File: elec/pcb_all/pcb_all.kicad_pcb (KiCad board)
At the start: 2 copper layers, 1 part, among them U1 Xiao_ESP32-C3

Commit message: did most pf power schematics
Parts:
- added IC1: BQ25176MDSGR, footprints:SON50P200X200X80-9N, F.Cu at (99.2, 59.5)
- added U2: BQ29700DSER, footprints:SON50P150X150X80-6N, F.Cu at (96.6, 71.2)

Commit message: did pcb layout for bucks, boost, imu, barometer, vibration module, need to continue batt protection
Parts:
- added B1: HD-EMC1003-3-LW27, footprints:PUI_HD-EMC1003-3-LW27, F.Cu at (89.1, 167.3)
- added BT1: Battery_Cell, Connector_JST:JST_XH_B2B-XH-A_1x02_P2.50mm_Vertical, F.Cu at (107.5, 103.0)
- added C1: 4.7uF, Capacitor_SMD:C_1206_3216Metric, F.Cu at (91.2, 127.5)
- added C10: 22uF, Capacitor_SMD:C_1206_3216Metric, F.Cu at (111.4, 124.8)
- added C11: 10uF, Capacitor_SMD:C_1206_3216Metric, F.Cu at (88.0, 106.8)
- added C12: 1uF, Capacitor_SMD:C_0603_1608Metric, F.Cu at (83.0, 40.0)
- added C13: 22uF, Capacitor_SMD:C_1206_3216Metric, F.Cu at (93.0, 100.5)
- added C14: 100nF, Capacitor_SMD:C_0603_1608Metric, F.Cu at (83.0, 42.6)
- added C15: 22uF, Capacitor_SMD:C_1206_3216Metric, F.Cu at (90.2, 100.5)
- added C16: 10uF, Capacitor_SMD:C_1206_3216Metric, F.Cu at (105.5, 43.0)
- added C17: 0.1uF, Capacitor_SMD:C_0603_1608Metric, F.Cu at (107.5, 165.5)
- added C18: 100nF, Capacitor_SMD:C_0603_1608Metric, F.Cu at (88.2, 145.8)
- added C19: 100nF, Capacitor_SMD:C_0603_1608Metric, F.Cu at (106.4, 151.6)
- added C2: 0.1uF, Capacitor_SMD:C_0603_1608Metric, F.Cu at (124.0, 101.0)
- added C20: 22uF, Capacitor_SMD:C_1206_3216Metric, F.Cu at (108.2, 162.2)
- added C21: 100nF, Capacitor_SMD:C_0603_1608Metric, F.Cu at (91.5, 148.8)
- added C22: 100nF, Capacitor_SMD:C_0603_1608Metric, F.Cu at (109.7, 148.3)
- added C3: 22uF, Capacitor_SMD:C_1206_3216Metric, F.Cu at (87.7, 130.8)
- added C4: 10uF, Capacitor_SMD:C_1206_3216Metric, F.Cu at (101.4, 125.1)
- added C5: 1uF, Capacitor_SMD:C_0603_1608Metric, F.Cu at (83.0, 35.0)
- added C6: 100nF, Capacitor_SMD:C_0201_0603Metric, F.Cu at (105.7, 127.8)
- added C7: 100nF, Capacitor_SMD:C_0603_1608Metric, F.Cu at (83.0, 37.5)
- added C8: 22uF, Capacitor_SMD:C_1206_3216Metric, F.Cu at (108.9, 124.8)
- added C9: 10uF, Capacitor_SMD:C_1206_3216Metric, F.Cu at (99.9, 46.3)
- added D1: ESD7351XV2T1G, footprints:SODFL1608X70N, F.Cu at (77.0, 53.8)
- added D2: LED, Capacitor_SMD:C_0603_1608Metric, F.Cu at (87.0, 35.0)
- added D3: LED, Capacitor_SMD:C_0603_1608Metric, F.Cu at (87.0, 37.5)
- added D4: LED, Capacitor_SMD:C_0603_1608Metric, F.Cu at (87.0, 40.0)
- added D5: ESD7351XV2T1G, footprints:SODFL1608X70N, F.Cu at (77.0, 56.1)
- added D6: LED, Capacitor_SMD:C_0603_1608Metric, F.Cu at (87.0, 42.6)
- added D7: SS14-M3_5AT, footprints:DIOM5127X229N, F.Cu at (104.3, 167.2)
- added IC2: AP63203WU-7, footprints:AP63203WU7, F.Cu at (105.2, 124.8)
- added IC3: BQ25176MDSGR, footprints:SON50P200X200X80-9N, F.Cu at (67.9, 67.1)
- added IC4: TPS61023DRLR, footprints:SOTFL50P160X60-6N, F.Cu at (87.8, 101.8)
- added IC5: BMP390, footprints:BMP390, F.Cu at (88.0, 149.2)
- added IC6: LSM6DSLTR, footprints:LSM6DSLTR, F.Cu at (106.2, 148.6)
- added J1: Conn_01x02, Connector_JST:JST_XH_B2B-XH-A_1x02_P2.50mm_Vertical, F.Cu at (104.3, 65.0)
- added J2: Conn_01x07, Connector_PinHeader_2.54mm:PinHeader_1x07_P2.54mm_Vertical, F.Cu at (63.4, 50.4)
- added L1: 2.2uH, Inductor_SMD:L_1008_2520Metric, F.Cu at (85.7, 126.8)
- added L2: 4.7uH, Inductor_SMD:L_1008_2520Metric, F.Cu at (106.4, 129.6)
- added L3: 1uH, Inductor_SMD:L_1008_2520Metric, F.Cu at (88.5, 104.3)
- added Q1: CSD16301Q2, footprints:CSD16301Q2, F.Cu at (126.5, 105.2)
- added Q2: CSD16301Q2, footprints:CSD16301Q2, F.Cu at (119.8, 105.2)
- added Q3: IRLML6344TRPBF, footprints:SOT95P237X112-3N, F.Cu at (108.0, 168.2)
- added R1: 34k, Resistor_SMD:R_0603_1608Metric, F.Cu at (89.4, 123.7)
- added R10: 10k, Resistor_SMD:R_0603_1608Metric, F.Cu at (91.0, 45.1)
- added R11: 680R, Resistor_SMD:R_0603_1608Metric, F.Cu at (91.0, 47.6)
- added R12: 10k, Resistor_SMD:R_0603_1608Metric, F.Cu at (91.0, 50.1)
- added R13: 604, Resistor_SMD:R_0603_1608Metric, F.Cu at (91.0, 52.6)
- added R14: 24.3k, Resistor_SMD:R_0603_1608Metric, F.Cu at (95.0, 32.5)
- added R15: 732k, Resistor_SMD:R_0603_1608Metric, F.Cu at (86.0, 100.0)
- added R16: 100k, Resistor_SMD:R_0603_1608Metric, F.Cu at (85.8, 102.3)
- added R17: 680R, Resistor_SMD:R_0603_1608Metric, F.Cu at (95.0, 40.0)
- added R18: 10k, Resistor_SMD:R_0603_1608Metric, F.Cu at (95.0, 42.6)
- added R19: 1k, Resistor_SMD:R_0603_1608Metric, F.Cu at (95.0, 45.1)
- added R2: 4.7k, Resistor_SMD:R_0603_1608Metric, F.Cu at (87.0, 47.6)
- added R20: 10k, Resistor_SMD:R_0603_1608Metric, F.Cu at (110.8, 165.5)
- added R21: 100R, Resistor_SMD:R_0603_1608Metric, F.Cu at (111.8, 168.2)
- added R22: 4.7k, Resistor_SMD:R_0603_1608Metric, F.Cu at (106.7, 144.6)
- added R3: R330, Resistor_SMD:R_0603_1608Metric, F.Cu at (126.0, 101.0)
- added R4: 4.7k, Resistor_SMD:R_0603_1608Metric, F.Cu at (87.0, 52.6)
- added R5: 64.9k, Resistor_SMD:R_0603_1608Metric, F.Cu at (87.9, 123.7)
- added R6: 5.1M, Resistor_SMD:R_0603_1608Metric, F.Cu at (121.8, 101.8)
- added R7: 5.1M, Resistor_SMD:R_0603_1608Metric, F.Cu at (118.8, 101.0)
- added R8: 2.2K, Resistor_SMD:R_0603_1608Metric, F.Cu at (128.0, 101.0)
- added R9: 10k, Resistor_SMD:R_0603_1608Metric, F.Cu at (91.0, 42.6)
- added TP1: TestPoint_2Pole, Connector_PinHeader_2.54mm:PinHeader_1x02_P2.54mm_Vertical, F.Cu at (105.0, 94.2)
- added TP2: TestPoint, Connector_PinHeader_2.54mm:PinHeader_1x01_P2.54mm_Vertical, F.Cu at (123.5, 97.0)
- added TP3: TestPoint_2Pole, Connector_PinHeader_2.54mm:PinHeader_1x02_P2.54mm_Vertical, F.Cu at (87.7, 118.2)
- added TP4: TestPoint, Connector_PinHeader_2.54mm:PinHeader_1x01_P2.54mm_Vertical, F.Cu at (130.8, 105.3)
- added TP5: TestPoint, Connector_PinHeader_2.54mm:PinHeader_1x01_P2.54mm_Vertical, F.Cu at (118.5, 97.8)
- added TP6: TestPoint_2Pole, Connector_PinHeader_2.54mm:PinHeader_1x02_P2.54mm_Vertical, F.Cu at (130.8, 97.7)
- added TP7: TestPoint_2Pole, Connector_PinHeader_2.54mm:PinHeader_1x02_P2.54mm_Vertical, F.Cu at (104.5, 118.2)
- added TP8: TestPoint_2Pole, Connector_PinHeader_2.54mm:PinHeader_1x02_P2.54mm_Vertical, F.Cu at (87.2, 94.2)
- IC1: value BQ25176MDSGR -> TPS629203QDRLRQ1; footprint footprints:SON50P200X200X80-9N -> footprints:SOTFL50P160X60-8N
- U1: value Xiao_ESP32-C3 -> BQ29700DSER; footprint footprints:Xiao_ESP32-C3 -> footprints:SON50P150X150X80-6N
- U2: value BQ29700DSER -> Xiao_ESP32-C3; footprint footprints:SON50P150X150X80-6N -> footprints:Xiao_ESP32-C3
- moved IC1 67.9 mm to (88.3, 126.5)
- moved U1 56.3 mm to (121.8, 100.0)
- moved U2 48.7 mm to (134.6, 40.8)
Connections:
- IC1 pad 1: unconnected-(IC1-IN-Pad1) -> Net-(IC1-FB/VSET)
- IC1 pad 3: unconnected-(IC1-BIAS-Pad3) -> +1V8
- IC1 pad 4: unconnected-(IC1-GND-Pad4) -> Net-(IC1-SW)
- IC1 pad 5: unconnected-(IC1-STAT-Pad5) -> GND
- IC1 pad 6: unconnected-(IC1-~{PG}-Pad6) -> +BATT
- IC1 pad 7: unconnected-(IC1-VSET-Pad7) -> +BATT
- IC1 pad 8: unconnected-(IC1-OUT-Pad8) -> Net-(IC1-MODE/S-CONF)
- U1 pad 2: unconnected-(U1-D1-Pad2) -> Net-(Q2-G)
- U1 pad 3: unconnected-(U1-D2-Pad3) -> Net-(Q1-G)
- U1 pad 4: unconnected-(U1-D3-Pad4) -> Net-(BT1--)
- U1 pad 5: unconnected-(U1-D4-Pad5) -> Net-(U1-BAT)
- U1 pad 6: unconnected-(U1-D5-Pad6) -> Net-(U1-V-)
- U2 pad 1: unconnected-(U2-NC-Pad1) -> /A (MIC)
- U2 pad 2: unconnected-(U2-COUT-Pad2) -> /BATT VOLTAGE
- U2 pad 3: unconnected-(U2-DOUT-Pad3) -> /INT1 (IMU)
- U2 pad 4: unconnected-(U2-VSS-Pad4) -> /PWM (Vibration)
- U2 pad 5: unconnected-(U2-BAT-Pad5) -> /SDA
- U2 pad 6: unconnected-(U2-V--Pad6) -> /SCL
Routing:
- net Net-(BT1--): track 0.00 -> 8.76 mm
- net +BATT: track 0.00 -> 8.76 mm
- net +3V3: track 0.00 -> 8.34 mm, vias 0 -> 4
- net Net-(Q1-G): track 0.00 -> 8.27 mm
- net /PWM (Vibration): track 0.00 -> 3.16 mm
- net Net-(IC4-FB): track 0.00 -> 2.90 mm
- net Net-(IC6-CS): track 0.00 -> 2.30 mm
- net Net-(Q3-G): track 0.00 -> 2.22 mm
- net Net-(IC2-BST): track 0.00 -> 1.95 mm
- net GND: vias 0 -> 9
- added copper zone on F.Cu, net +1V8
- added copper zone on B.Cu, net +3V3
- added copper zone on F.Cu, net +3V3
- added copper zone on F.Cu, net +5V
- added copper zone on F.Cu, net +BATT
- added copper zone on B.Cu, net GND
- added copper zone on F.Cu, net GND
- added copper zone on F.Cu, net Net-(D7-A)
- added copper zone on F.Cu, net Net-(IC2-SW)
- added copper zone on F.Cu, net Net-(IC4-SW)
- added copper zone on F.Cu, net Net-(Q2-G)
- added copper zone on F.Cu, net Net-(U1-BAT)
- added copper zone on F.Cu, net Net-(U1-V-)
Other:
- board text added: "1v8 Buck"
- board text added: "3v3 Buck"
- board text added: "5v Boost"
- board text added: "Barometer Module"
- board text added: "Battery"
- board text added: "Battery Protection"
- board text added: "IMU Module"
- board text added: "Vibration Module"

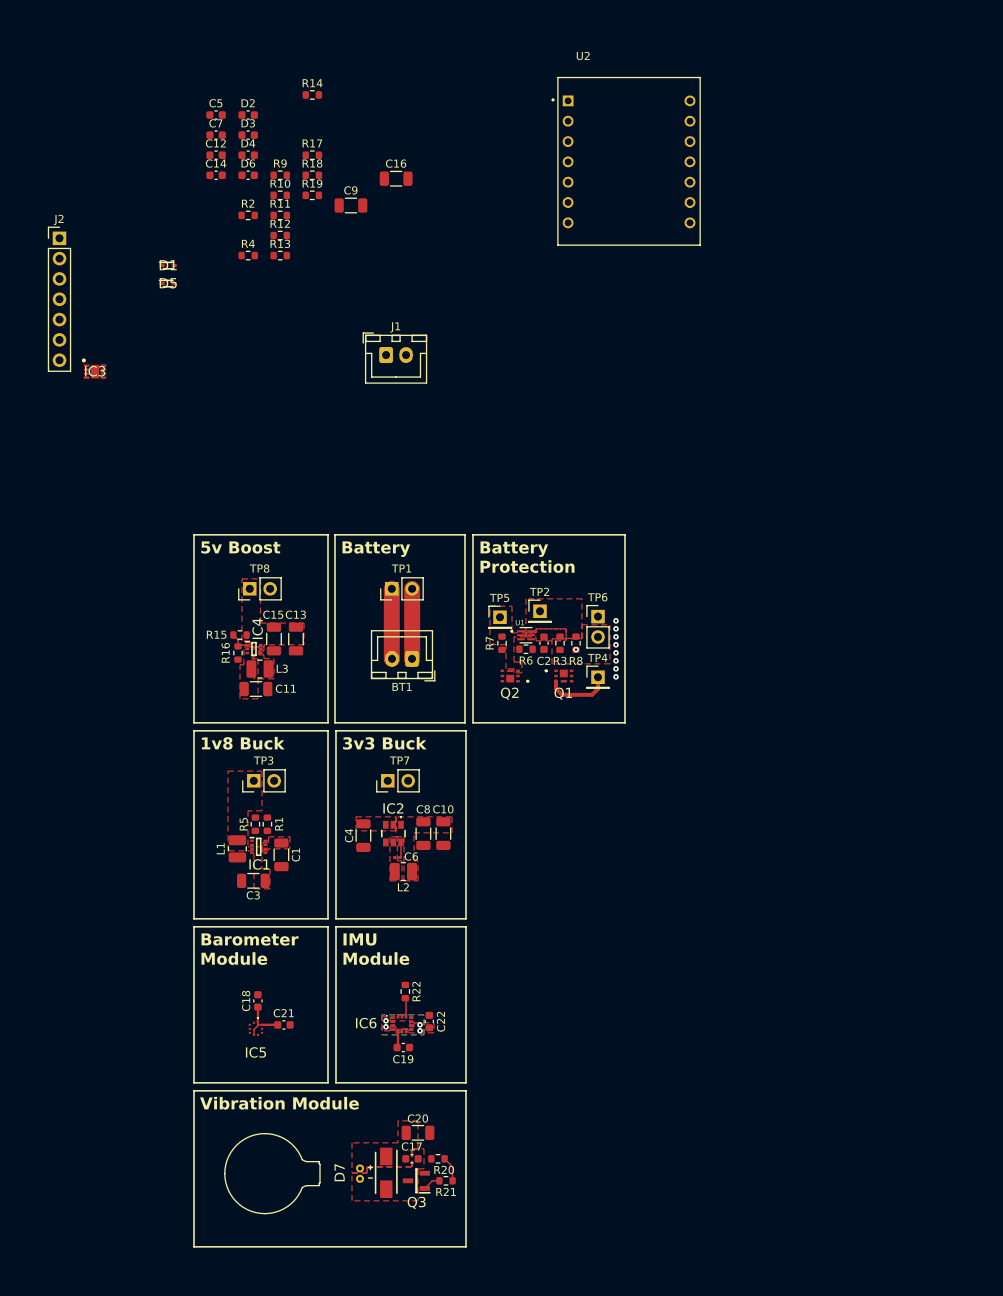
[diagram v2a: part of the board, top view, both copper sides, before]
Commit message: complaeted placement of all components, pending traces to mcu
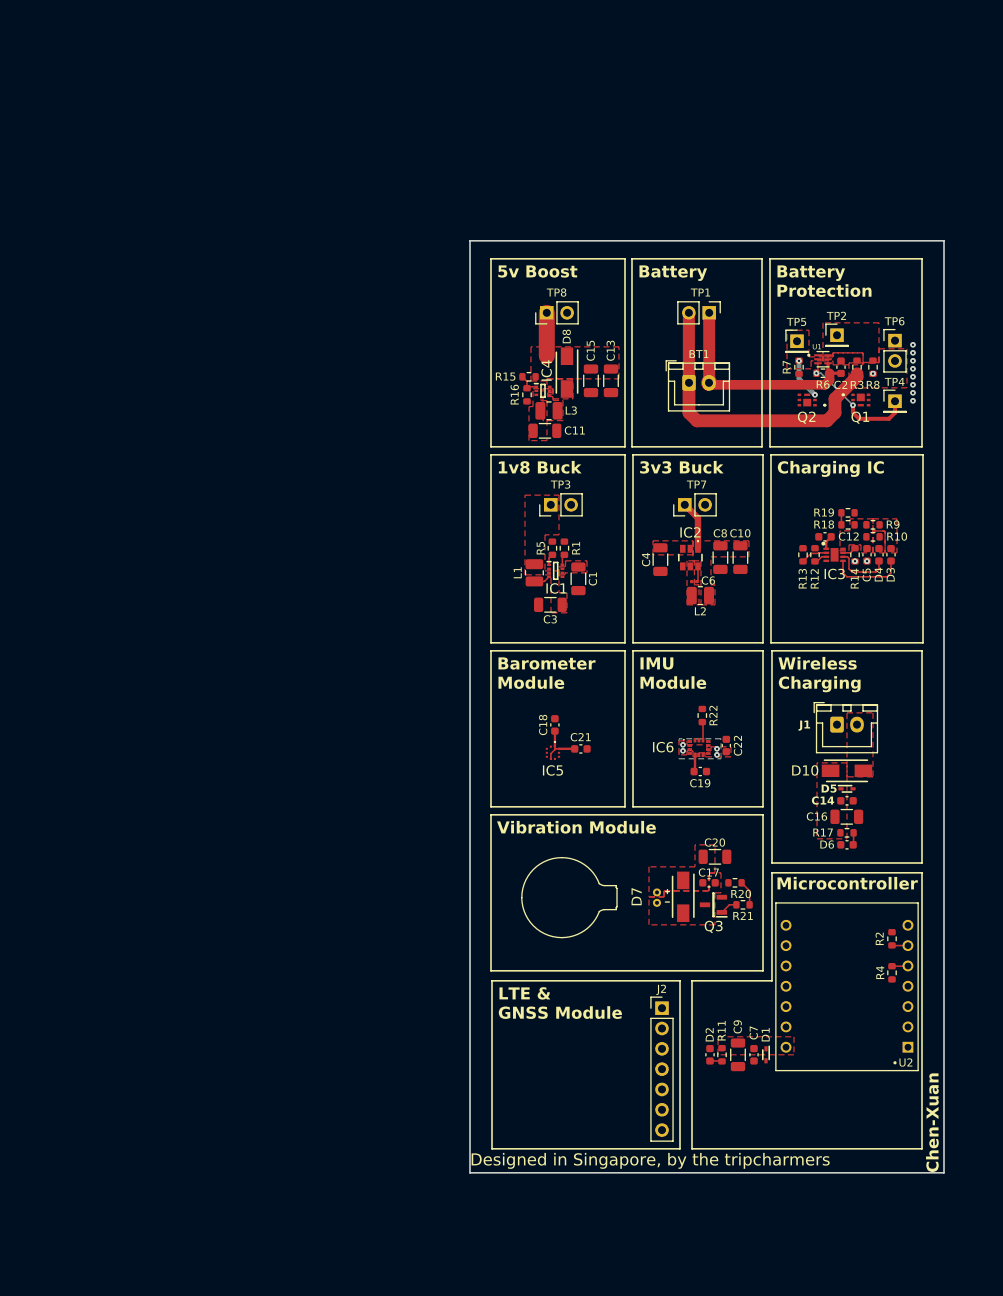
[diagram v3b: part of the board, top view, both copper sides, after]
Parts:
- added D10: SS14-M3_5AT, footprints:DIOM5127X229N, F.Cu at (161.9, 117.0)
- added D8: SS14-M3_5AT, footprints:DIOM5127X229N, F.Cu at (126.9, 67.2)
- moved C7 133.2 mm to (150.2, 152.5), turned to -90 degrees
- moved D2 130.9 mm to (144.7, 152.5), turned to -90 degrees
- moved D1 123.8 mm to (151.8, 152.5), turned to -90 degrees
- moved J2 122.2 mm to (138.8, 146.7)
- moved R2 121.1 mm to (167.5, 138.0), turned to -90 degrees
- moved R4 120.5 mm to (167.5, 142.2), turned to 90 degrees
- moved R11 118.6 mm to (146.2, 152.5), turned to -90 degrees
- moved C9 116.7 mm to (148.2, 152.5), turned to -90 degrees
- moved D6 112.3 mm to (161.9, 126.2)
- moved C14 111.1 mm to (161.9, 120.8)
- moved R17 107.9 mm to (161.9, 124.8)
- moved U2 106.7 mm to (161.9, 144.0), turned to 180 degrees
- moved D5 105.8 mm to (161.9, 119.2)
- moved C5 98.2 mm to (164.4, 90.0), turned to -90 degrees
- moved C16 97.7 mm to (161.8, 122.8)
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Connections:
- IC4 pad 6: +5V -> Net-(D8-A)
- J1 pad 2: +5V -> Net-(D10-A)
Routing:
- net +BATT: track 8.76 -> 37.6 mm
- net Net-(BT1--): track 8.76 -> 27.5 mm
- net Net-(D3-K): track 0.00 -> 9.39 mm
- net Net-(Q1-G): track 8.27 -> 15.8 mm, vias 0 -> 2
- net Net-(D4-K): track 0.00 -> 7.19 mm
- net +5V: track 0.00 -> 7.18 mm
- net +3V3: track 8.34 -> 14.5 mm
- net Net-(Q2-G): track 0.00 -> 5.08 mm, vias 0 -> 2
- net Net-(IC3-ISET): track 0.00 -> 3.35 mm
- net Net-(IC1-SW): track 0.00 -> 2.06 mm
- net /SDA: track 0.00 -> 2.01 mm
- net /SCL: track 0.00 -> 2.01 mm
- net Net-(IC3-VSET): track 0.00 -> 1.74 mm
- net Net-(IC3-BIAS): track 0.00 -> 1.64 mm
- net Net-(D6-A): track 0.00 -> 1.52 mm
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- added copper zone on F.Cu, net Net-(D10-A)
- added copper zone on F.Cu, net Net-(D3-A)
- added copper zone on F.Cu, net Net-(D4-A)
- added copper zone on F.Cu, net Net-(D8-A)
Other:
- board outline added: 59.2 x 116.5 mm
- board text added: "Charging IC"
- board text added: "Chen-Xuan"
- board text added: "Designed in Singapore, by the tripcharmers"
- board text added: "LTE & GNSS Module"
- board text added: "Microcontroller"
- board text added: "Wireless Charging"

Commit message: completed pcb?
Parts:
- added R23: 10k, Resistor_SMD:R_0603_1608Metric, F.Cu at (156.5, 139.7)
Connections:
- Q1 pad 1: (no net) -> Net-(BT1--)
- Q1 pad 2: (no net) -> Net-(Q1-D)
- Q2 pad 1: (no net) -> Net-(Q1-D)
- Q2 pad 2: (no net) -> GND
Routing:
- net +5V: track 7.18 -> 160.3 mm
- net +3V3: track 14.5 -> 118.0 mm, vias 4 -> 7
- net /BATT VOLTAGE: track 1.50 -> 68.9 mm, vias 0 -> 3
- net /SCL: track 2.01 -> 68.3 mm, vias 0 -> 2
- net /SDA: track 2.01 -> 66.5 mm, vias 0 -> 2
- net +BATT: track 37.6 -> 100.1 mm, vias 0 -> 20
- net /RX (SIM7600G-H): track 0.00 -> 58.0 mm
- net /INT (BAROMETER): track 0.00 -> 52.8 mm, vias 0 -> 1
- net /INT1 (IMU): track 0.00 -> 46.7 mm, vias 0 -> 1
- net /TX (SIM7600G-H): track 0.00 -> 40.7 mm
- net Net-(Q1-D): track 0.00 -> 28.8 mm, vias 0 -> 8
- net /PWM (Vibration): track 3.16 -> 30.6 mm, vias 0 -> 2
- net /SLEEP (SIM7600G-H): track 0.00 -> 21.0 mm, vias 0 -> 1
- net Net-(BT1--): track 27.5 -> 38.4 mm, vias 0 -> 8
- net Net-(Q1-G): track 15.8 -> 17.4 mm
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- added copper zone on B.Cu, net +BATT
- added copper zone on B.Cu, net Net-(BT1--)
- added copper zone on F.Cu, net Net-(BT1--)
- added copper zone on B.Cu, net Net-(Q1-D)
- added copper zone on F.Cu, net Net-(Q1-D)

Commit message: made some stuff look better
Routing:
- net Net-(Q1-G): track 17.4 -> 18.9 mm
- net Net-(Q1-D): track 28.8 -> 30.2 mm
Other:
- board text added: "designed by the tripcharmers"
- board text added: "revision 1 28/4/25"
- board text removed: "Designed in Singapore, by the tripcharmers"

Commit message: cleaned up some more stuff
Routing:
- net +3V3: track 118.0 -> 118.5 mm

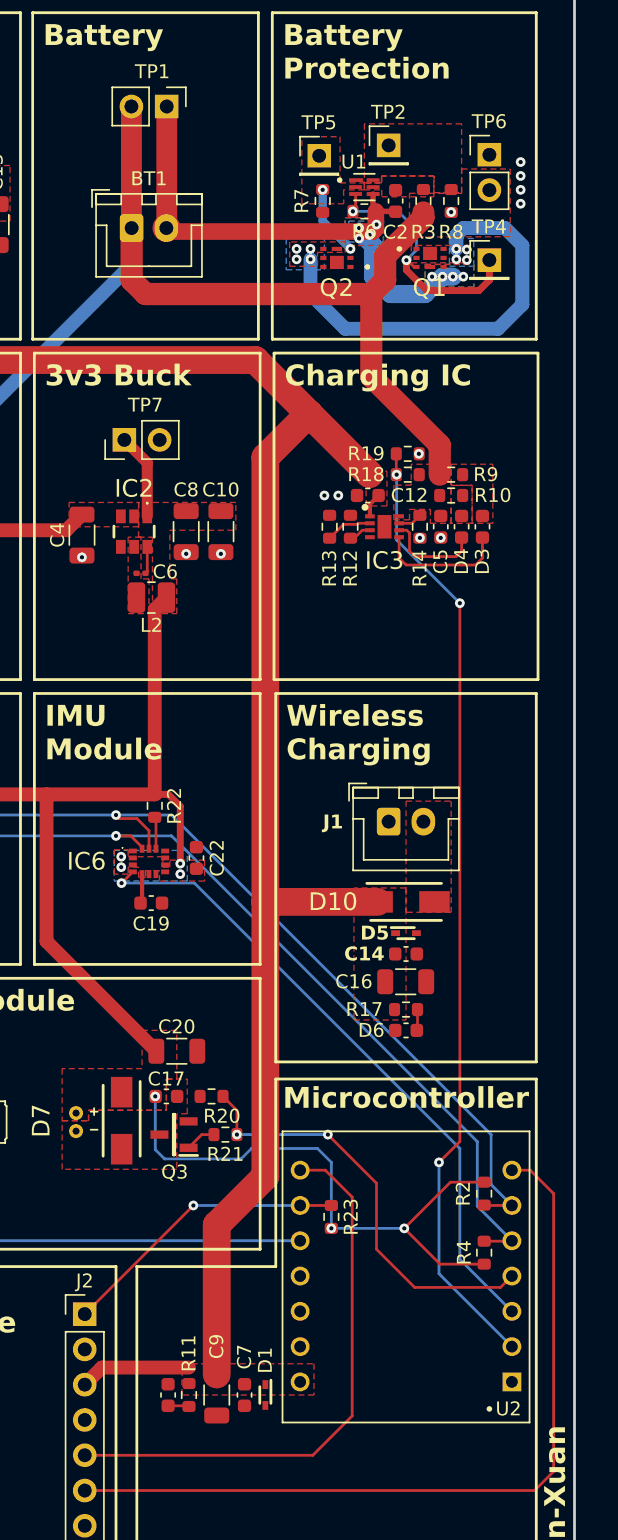
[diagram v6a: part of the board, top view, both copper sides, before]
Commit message: made jlcdfm slightly happier
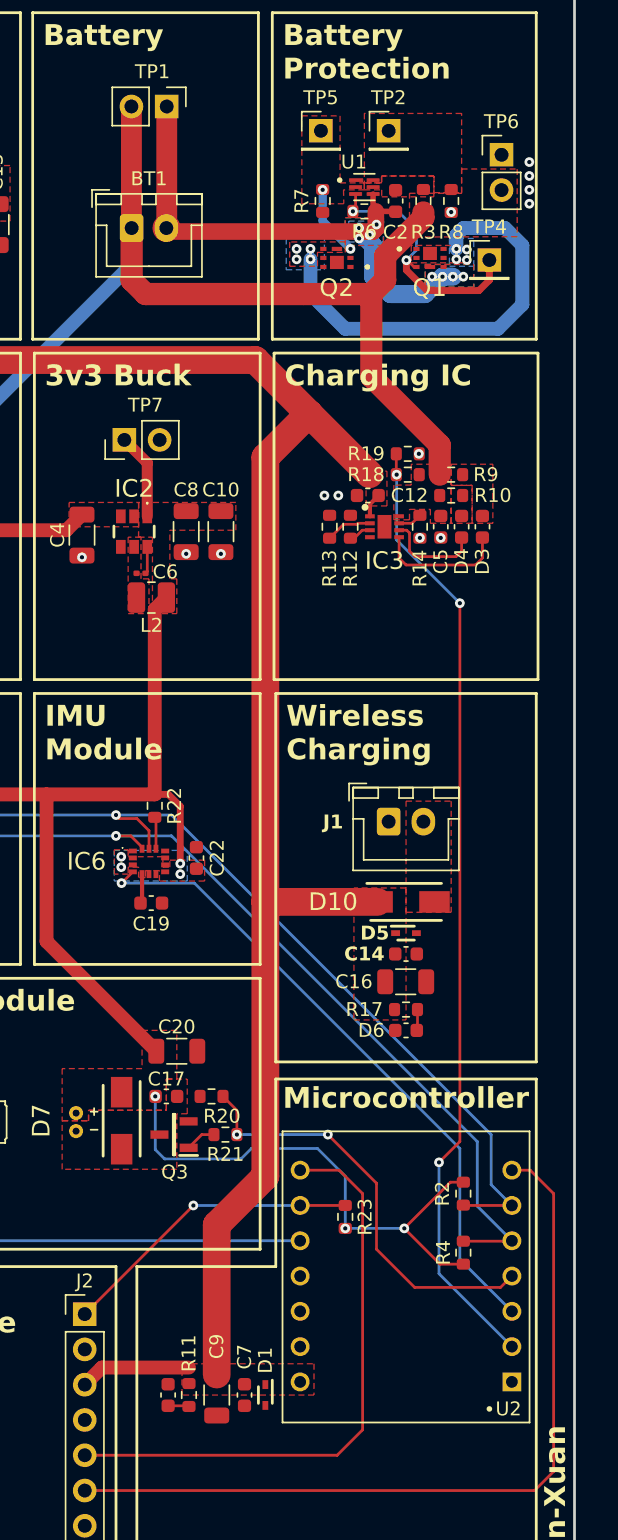
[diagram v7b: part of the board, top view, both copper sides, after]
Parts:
- moved TP5 1.80 mm to (155.8, 61.5)
- moved R2 1.50 mm to (166.0, 138.0)
- moved R4 1.50 mm to (166.0, 142.2)
- moved TP2 1.05 mm to (160.6, 61.5)
- moved R23 1.00 mm to (157.5, 139.7)
- moved TP6 0.88 mm to (168.8, 63.2)
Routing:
- net +3V3: track 118.5 -> 115.0 mm
- net /TX (SIM7600G-H): track 40.7 -> 43.0 mm
- net /SDA: track 66.5 -> 68.0 mm
- net /SCL: track 68.3 -> 69.8 mm
- net /SLEEP (SIM7600G-H): track 21.0 -> 22.0 mm
